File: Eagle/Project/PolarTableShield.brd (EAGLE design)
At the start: 56 x 59.7 mm, 42 parts, among them IC2 LM358D, J1 Pi Power Jack, J10 LED + Radio, J2 Header - Right angled, female, J3 Pi Connection, J5 IR Sensors, J6 Switch A + B, J7 Switch C + D, J8 Switch E + F, Q1 BC337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

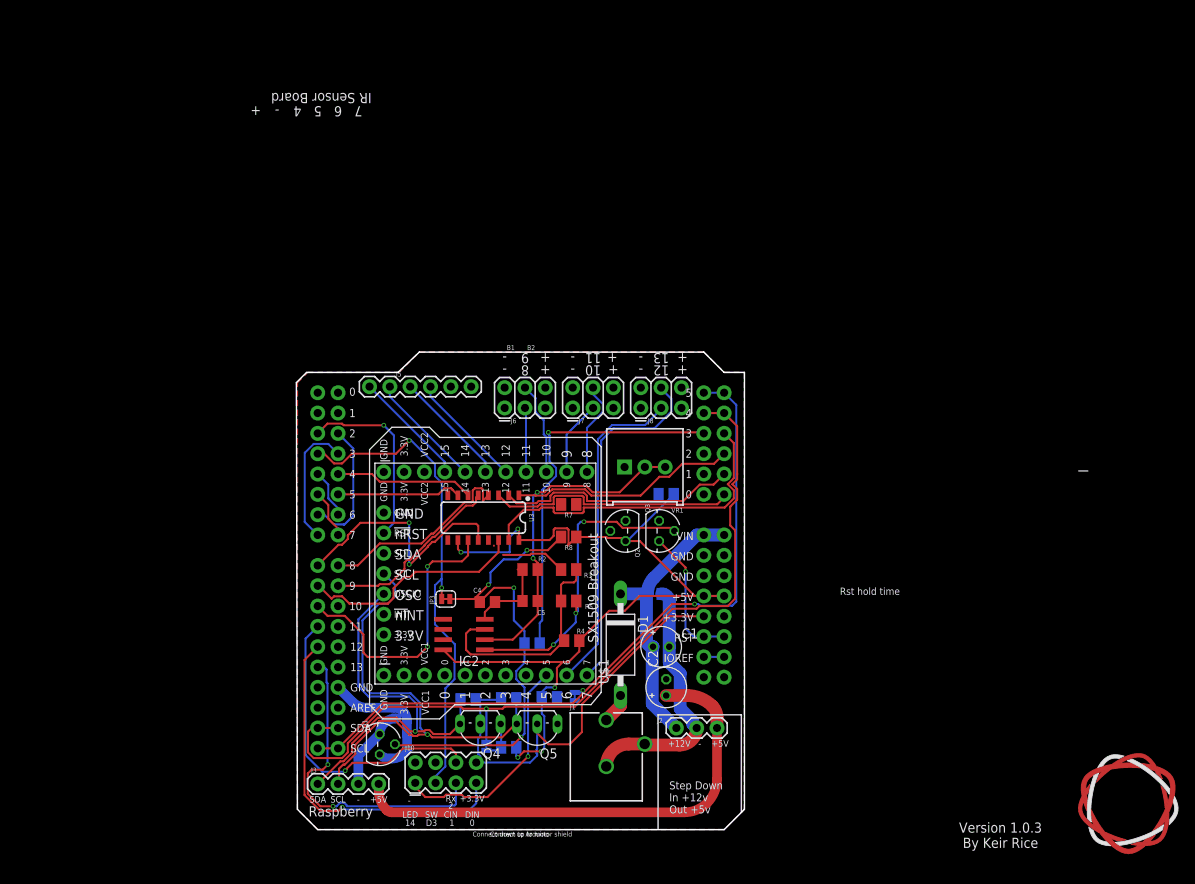
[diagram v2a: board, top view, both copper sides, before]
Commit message: Layed out existing design. Added headers for all pins.
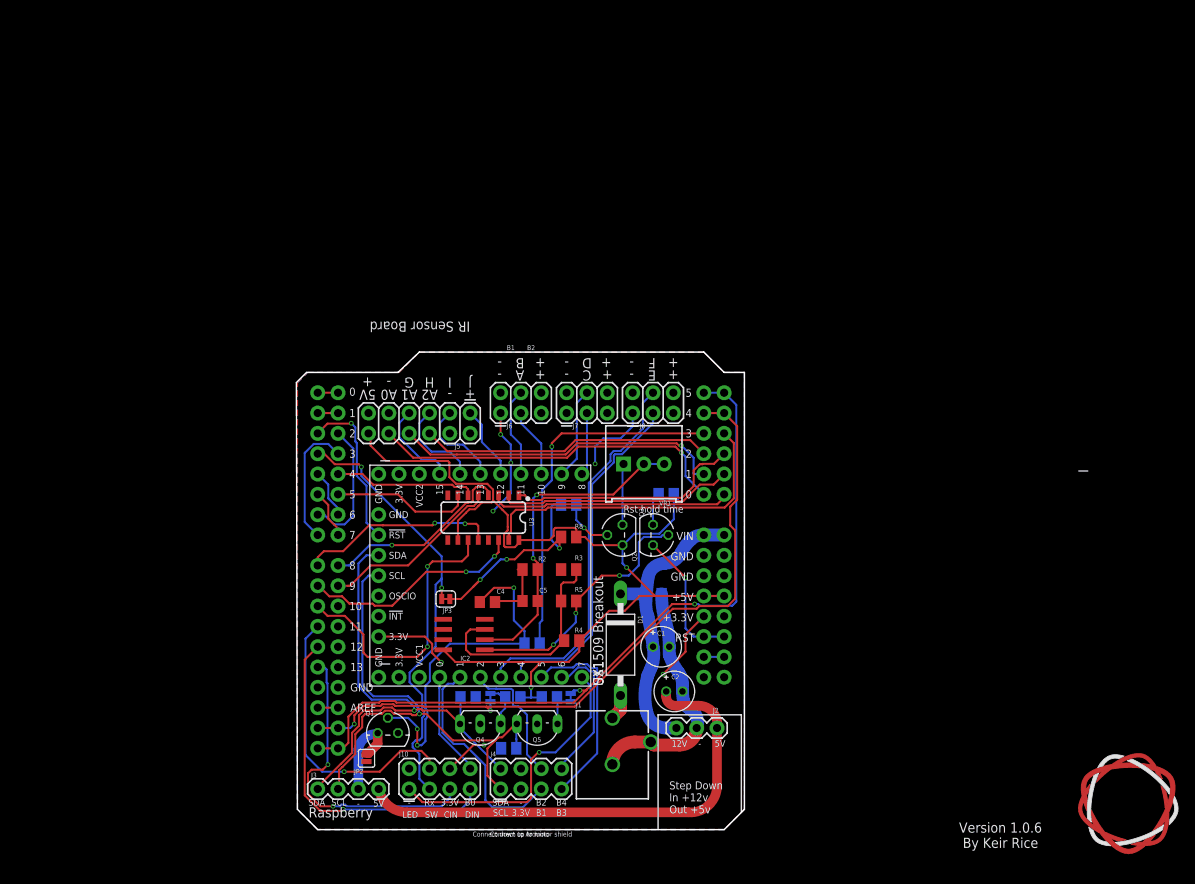
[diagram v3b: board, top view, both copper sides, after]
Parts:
- added J4: (no value), keir_library:2X4
- J5: device SparkFun-Connectors:1X06 -> keir_library:2X6
- moved JP2 6.76 mm to (8.64, 8.92), flipped to the top, turned to 270 degrees
- moved R6 6.24 mm to (26.9, 16.5)
- moved R11 6.22 mm to (26.4, 10.2)
- moved JP5 6.12 mm to (24.1, 16.5), turned to 270 degrees
- moved J5 3.30 mm to (21.6, 52.1)
- moved Q1 1.73 mm to (11.3, 12.1), turned to 0 degrees
- moved J8 1.20 mm to (41.9, 52.1)
- moved C2 1.14 mm to (47.1, 17.3), turned to 0 degrees
- moved J10 1.08 mm to (17.8, 6.35)
- moved J7 0.99 mm to (33.7, 52.1)
- moved Q3 0.92 mm to (44.5, 36.8)
- moved J6 0.81 mm to (25.4, 52.1)
- moved J1 0.80 mm to (39.4, 0.25)
- moved U$1 0.68 mm to (22.9, 31.8)
- moved Q2 0.64 mm to (40.6, 36.8)
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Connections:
- removed net B7: U$1.O0
- new net B0: J10.8, U$1.O0
- net 3.3V: now also J10.6, J4.3, J5.11, J5.2; no longer J10.8, J5.1
- net 5V: now also J5.12
- net A0: now also J5.10
- net A1: now also J5.8
- net A2: now also J5.6
- net B1: now also J4.5
- net B2: now also J4.6
- net B3: now also J4.7, U$1.O5; no longer U$1.O3
- net B4: now also J4.8, U$1.O6; no longer U$1.O4
- net D11_RXDATA: now also J10.4; no longer J10.6
- net GND: now also J4.4, J5.4, J5.9; no longer C2.-, J5.2
- net IR_G: now also J5.7; no longer J5.6
- net IR_I: now also J5.3; no longer J5.4
- net IR_J: now also J5.1; no longer J5.3
- net N$6: now also C2.-
- net SCL_3V: now also J4.1
- net SDA_3V: now also J4.2, U$1.I5; no longer U$1.I3
- net SW_A: now also U$1.O10; no longer U$1.O11
- net SW_B: now also U$1.O11; no longer U$1.O10
- net SW_C: now also U$1.O8; no longer U$1.O9
- net SW_D: now also U$1.O9; no longer U$1.O8
- net SW_E: now also U$1.O4; no longer U$1.O6
- net SW_F: now also U$1.O3; no longer U$1.O7
- net WAKE_LED: now also U$1.O7; no longer U$1.O5
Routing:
- net A0: track 0.00 -> 45.1 mm, vias 0 -> 1
- net A1: track 0.00 -> 41.3 mm, vias 0 -> 1
- net A2: track 0.00 -> 36.5 mm
- net 3.3V: track 55.0 -> 24.7 mm, vias 0 -> 3
- net B1: track 0.00 -> 28.0 mm
- net B3: track 0.00 -> 24.8 mm
- net B4: track 0.00 -> 18.6 mm
- net B2: track 0.00 -> 16.6 mm
- net 5V: track 107.6 -> 120.7 mm, vias 5 -> 2
- net B0: track 0.00 -> 13.1 mm
- net SDA: track 101.1 -> 88.7 mm, vias 1 -> 2
- net SDA_3V: track 51.1 -> 63.3 mm
- net $N99: track 17.9 -> 26.8 mm, vias 2 -> 3
- net N$7: track 0.00 -> 7.66 mm
- net WAKE_LED: track 28.6 -> 36.0 mm
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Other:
- board text added: "12V"
- board text added: "5V"
- board text added: "A"
- board text added: "A0"
- board text added: "A1"
- board text added: "A2"
- board text added: "B"
- board text added: "B0"
- board text added: "B1"
- board text added: "B2"
- board text added: "B3"
- board text added: "B4"
- board text added: "C"
- board text added: "D"
- board text added: "E"
- board text added: "F"
- board text added: "G"
- board text added: "H"
- board text added: "I"
- board text added: "J"
- board text added: "Version 1.0.6 By Keir Rice"
- board text removed: "+12V"
- board text removed: "14"
- board text removed: "15"
- board text removed: "D3"
- board text removed: "IOREF"
- board text removed: "OSC"
- board text removed: "VCC1"
- board text removed: "VCC2"
- board text removed: "Version 1.0.3 By Keir Rice"
- board text removed: "nINT"
- board text removed: "nRST"

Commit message: Layout and added frame.
Added status lights.
Matched trace lengths on the I2C bus.
Added logo.
Fixed up I2C connection on the SX1509 pins.
Added better labels and descriptions.
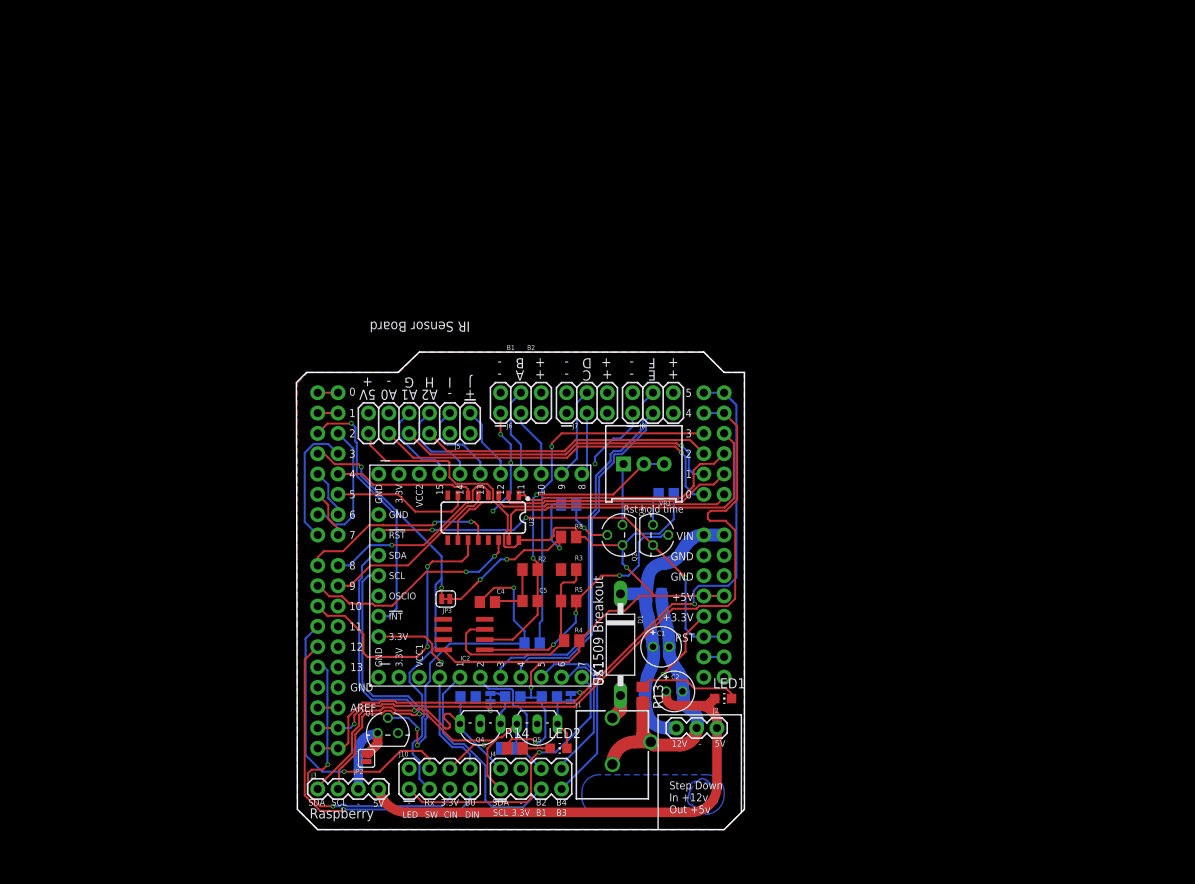
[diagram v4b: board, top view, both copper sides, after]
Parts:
- removed U$2: (no value), keir_library:TRI_LOGO_TOP_15MM
- added LED1, LED2: (no value), led:CHIP-LED0805
- added R13, R14: 1k, rcl:M0805
- added U$3: (no value), keir_library:TRI_LOGO_BOTTOM_5MM
- B1: value Connect down to Arduino -> (none)
- B2: value Connect up to motor shield -> (none)
- JP2: value Bypass Power Control -> (none)
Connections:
- new net N$10: LED2.A, R14.2
- new net N$9: LED1.C, R13.1
- net !INT: now also U$1.I2; no longer U$1.I6
- net !RES: now also U$1.I6
- net 5V: now also R14.1
- net 5V_SUPPLY: now also LED1.A
- net N$6: now also R13.2
- net SCL_5V: now also LED2.C
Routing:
- net !RES: track 17.3 -> 54.0 mm, vias 1 -> 3
- net !INT: track 20.1 -> 32.9 mm
- net N$9: track 0.00 -> 12.7 mm
- net 5V: track 120.7 -> 131.8 mm, vias 2 -> 3
- net N$6: track 30.4 -> 35.8 mm
- net SDA: track 88.7 -> 93.2 mm
- net SCL_5V: track 5.26 -> 8.79 mm
- net N$10: track 0.00 -> 3.52 mm
- net SDA_3V: track 63.3 -> 66.1 mm
- net 5V_SUPPLY: track 60.6 -> 63.0 mm
- net SCL: track 93.7 -> 92.4 mm
- net GND: track 31.5 -> 30.7 mm
- net A0: track 45.1 -> 45.8 mm
- net B0: track 13.1 -> 13.8 mm
- added copper zone on layer 16, net LOGO
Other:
- board text added: "Polar Controller"
- board text added: "Short JP2 to disable control of Pi Power from Arduino"
- board text added: "Short JP3 to enable hard reset by switch."
- board text added: "UR1 adjusts the hold time for reset"
- board text added: "Version 1.0.8 By Keir Rice"
- board text removed: "Enable JP3 for hard reset by switch."
- board text removed: "Pi power control. Connect 1-3 & 2-4 for soft switch via pin 15. Connect 3-5 & 4-6 for always on. Pin 15 routed to J4 connector."
- board text removed: "Version 1.0.6 By Keir Rice"

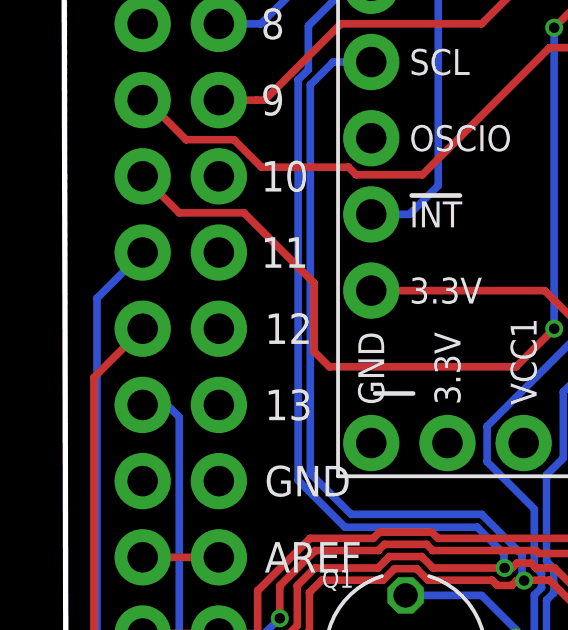
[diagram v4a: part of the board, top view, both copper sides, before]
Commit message: Moved the LED drive connection onto hardware SPI pins.
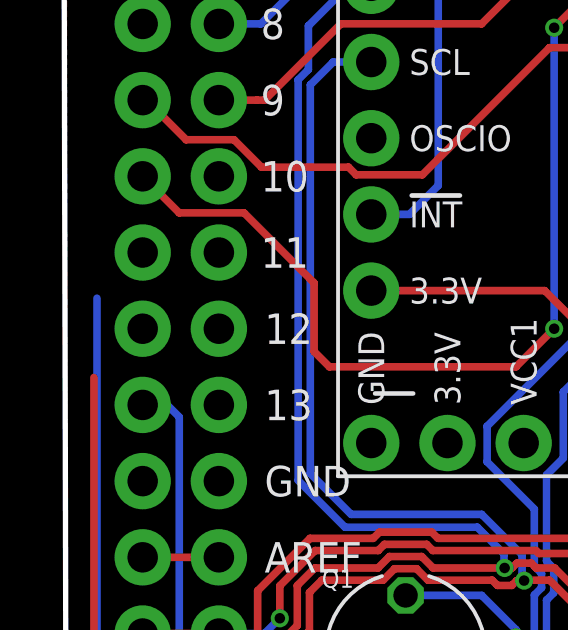
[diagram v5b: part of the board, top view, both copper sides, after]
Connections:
- removed net D11_RXDATA: B1.D11, J10.4
- removed net D12_SDIN: B1.D12, J10.7
- new net D11_SDIN: B1.D11, J10.7
- new net D12_RXDATA: B1.D12, J10.4
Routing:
- net D12_SDIN: track 42.7 -> 0.00 mm, vias 1 -> 0
- net D11_SDIN: track 0.00 -> 40.4 mm, vias 0 -> 1
- net D11_RXDATA: track 35.8 -> 0.00 mm, vias 1 -> 0
- net D12_RXDATA: track 0.00 -> 33.6 mm, vias 0 -> 1
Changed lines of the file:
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@@
 <wire x1="22.7028875" y1="32.2278875" x2="21.082" y2="32.2278875" width="0.254" layer="16"/>
 </signal>
-<signal name="D11_RXDATA" class="4">
-<contactref element="B1" pad="D11"/>
-<wire x1="2.54" y1="25.4" x2="1.016" y2="23.876" width="0.254" layer="16"/>
+<signal name="D12_RXDATA" class="4">
 <wire x1="1.016" y1="23.876" x2="1.016" y2="9.3247875" width="0.254" layer="16"/>
 <wire x1="1.016" y1="9.3247875" x2="3.1017875" y2="7.239" width="0.254" layer="16"/>
@@
 <wire x1="16.51" y1="7.62" x2="16.51" y2="8.8265" width="0.254" layer="1"/>
 <wire x1="16.51" y1="8.8265" x2="15.494" y2="9.8425" width="0.254" layer="1"/>
-</signal>
-<signal name="D12_SDIN" class="4">
 <contactref element="B1" pad="D12"/>
-<contactref element="J10" pad="7"/>
-<wire x1="21.59" y1="5.08" x2="21.59" y2="3.683" width="0.254" layer="16"/>
-<wire x1="2.8674" y1="2.3396" x2="5.5146" y2="2.3396" width="0.254" layer="1"/>
-<wire x1="5.5146" y1="2.3396" x2="5.715" y2="2.54" width="0.254" layer="1"/>
-<via x="5.715" y="2.54" extent="1-16" drill="0.35"/>
-<wire x1="21.59" y1="3.683" x2="20.4216" y2="2.5146" width="0.254" layer="16"/>
-<wire x1="20.4216" y1="2.5146" x2="5.9878875" y2="2.5146" width="0.254" layer="16"/>
-<wire x1="5.9878875" y1="2.5146" x2="5.9624875" y2="2.54" width="0.254" layer="16"/>
-<wire x1="5.9624875" y1="2.54" x2="5.715" y2="2.54" width="0.254" layer="16"/>
-<wire x1="2.54" y1="22.86" x2="0.9144" y2="21.2344" width="0.254" layer="1"/>
-<wire x1="0.9144" y1="4.2926" x2="2.8674" y2="2.3396" width="0.254" layer="1"/>
-<wire x1="0.9144" y1="21.2344" x2="0.9144" y2="4.2926" width="0.254" layer="1"/>
+<wire x1="1.016" y1="23.876" x2="2.54" y2="22.86" width="0" layer="19" extent="16-16"/>
 </signal>
 <signal name="D13_SCIN" class="4">
@@
 <wire x1="29.911775" y1="10.16" x2="28.128" y2="10.16" width="0.254" layer="1"/>
 </signal>
+<signal name="D11_SDIN">
+<contactref element="B1" pad="D11"/>
+<contactref element="J10" pad="7"/>
+<wire x1="21.59" y1="5.08" x2="21.59" y2="3.683" width="0.254" layer="16"/>
+<wire x1="2.8674" y1="2.3396" x2="5.5146" y2="2.3396" width="0.254" layer="1"/>
+<wire x1="5.5146" y1="2.3396" x2="5.715" y2="2.54" width="0.254" layer="1"/>
+<via x="5.715" y="2.54" extent="1-16" drill="0.35"/>
+<wire x1="21.59" y1="3.683" x2="20.4216" y2="2.5146" width="0.254" layer="16"/>
+<wire x1="20.4216" y1="2.5146" x2="5.9878875" y2="2.5146" width="0.254" layer="16"/>
+<wire x1="5.9878875" y1="2.5146" x2="5.9624875" y2="2.54" width="0.254" layer="16"/>
+<wire x1="5.9624875" y1="2.54" x2="5.715" y2="2.54" width="0.254" layer="16"/>
+<wire x1="0.9144" y1="4.2926" x2="2.8674" y2="2.3396" width="0.254" layer="1"/>
+<wire x1="0.9144" y1="21.2344" x2="0.9144" y2="4.2926" width="0.254" layer="1"/>
+<wire x1="0.9144" y1="21.2344" x2="2.54" y2="25.4" width="0" layer="19" extent="1-1"/>
+</signal>
 </signals>
